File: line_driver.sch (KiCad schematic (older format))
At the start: 26 parts, among them J7 DRV632

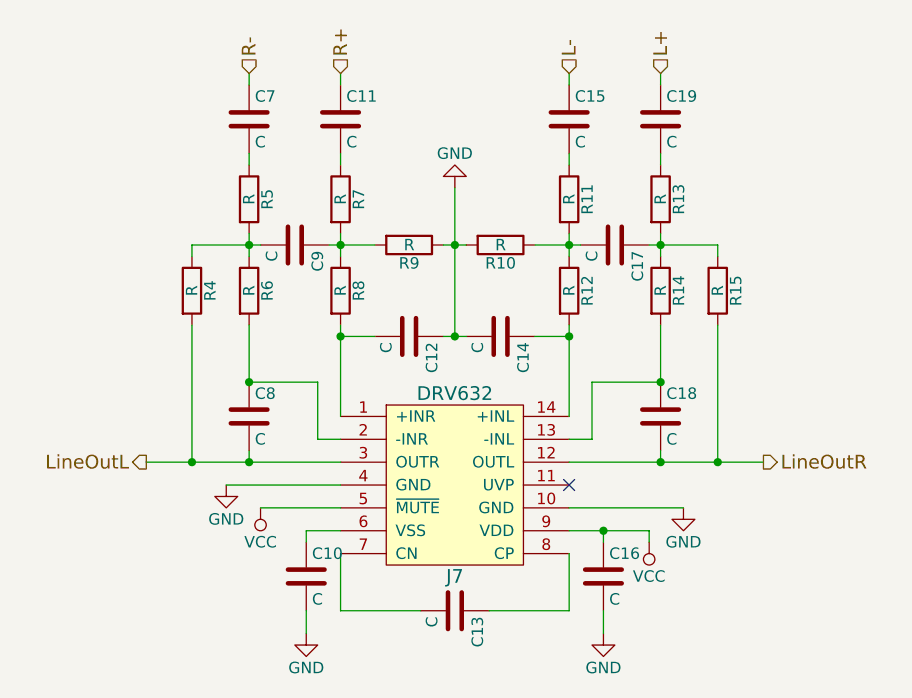
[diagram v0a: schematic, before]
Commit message: Simple line driver
Contains minimal components. no 2nd order low pass filter on input.
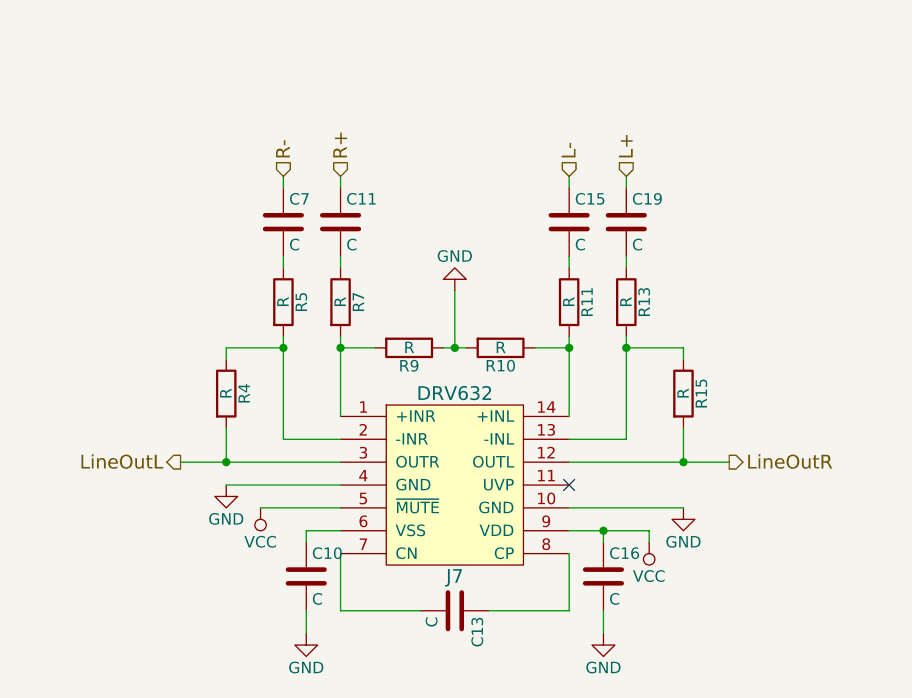
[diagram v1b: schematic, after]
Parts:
- removed C12, C14, C17, C18, C8, C9: C, symbol C
- removed R12, R14, R6, R8: R, symbol R
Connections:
- net at J7.1 (+INR): now also R7.2, R9.2
- net at J7.13 (-INL): now also R13.2, R15.1
- net at J7.14 (+INL): now also R10.1, R11.2
- net at J7.2 (-INR): now also R4.1, R5.2
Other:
- moved on the sheet: C11, C15, C19, C7, R10, R11, R13, R15, R4, R5, R7, R9

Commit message: Apparently something wasn't saved.
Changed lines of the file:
@@
 	5150 3950 5150 4050
 Wire Wire Line
-	6300 3600 6450 3600
-Wire Wire Line
-	6450 3600 6650 3600
+	6300 3600 6650 3600
 Wire Wire Line
 	6450 3950 6450 4050
@@
 	5300 3400 4800 3400
 Wire Wire Line
-	6300 3300 6800 3300
+	6300 3300 7000 3300
 Wire Wire Line
-	6800 3300 7000 3300
+	4600 3300 5300 3300
 Wire Wire Line
-	4600 3300 4800 3300
-Wire Wire Line
-	4800 3300 5300 3300
-Wire Wire Line
-	5750 2800 5800 2800
-Wire Wire Line
-	5800 2800 5850 2800
+	5750 2800 5850 2800
 Connection ~ 5800 2800
 Wire Wire Line
-	6300 2750 6300 2800
+	6300 2750 6300 3100
 Wire Wire Line
-	6300 2800 6300 3100
-Wire Wire Line
-	5300 2750 5300 2800
-Wire Wire Line
-	5300 2800 5300 3100
+	5300 2750 5300 3100
 Wire Wire Line
 	5300 2800 5450 2800
@@
 	6550 2400 6550 2450
 Wire Wire Line
-	6550 2750 6550 2800
+	6550 2750 6550 3200
 Wire Wire Line
-	6550 2800 6550 3200
-Wire Wire Line
-	5050 2750 5050 2800
-Wire Wire Line
-	5050 2800 5050 3200
+	5050 2750 5050 3200
 Wire Wire Line
 	6800 2800 6800 2850
